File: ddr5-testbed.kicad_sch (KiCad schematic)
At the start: 2 parts

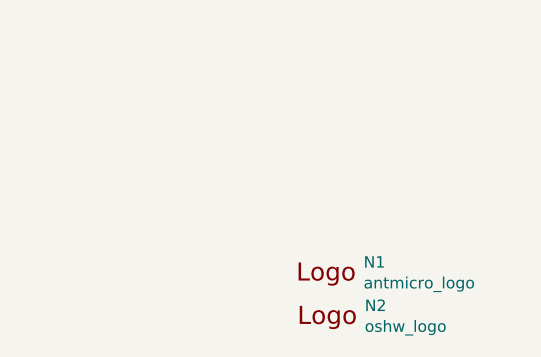
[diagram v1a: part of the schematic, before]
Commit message: Introduce component standardization
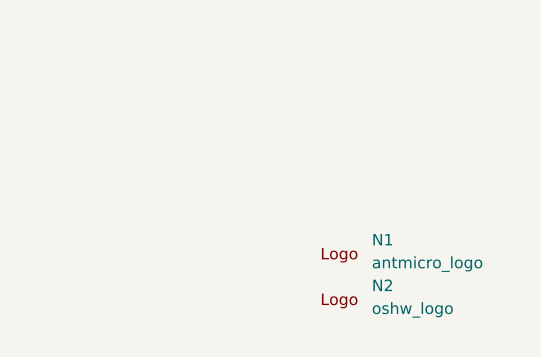
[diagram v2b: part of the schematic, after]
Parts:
- N1, N2: Author (none) -> Antmicro; License (none) -> Apache-2.0
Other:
- moved on the sheet: N1, N2
